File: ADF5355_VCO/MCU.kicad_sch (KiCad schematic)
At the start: 34 parts, among them SW2 SW_Push, SW3 SW_DPDT_x2, U2 STM32L433CCTx, Y1 8MHz, Y2 32kHz

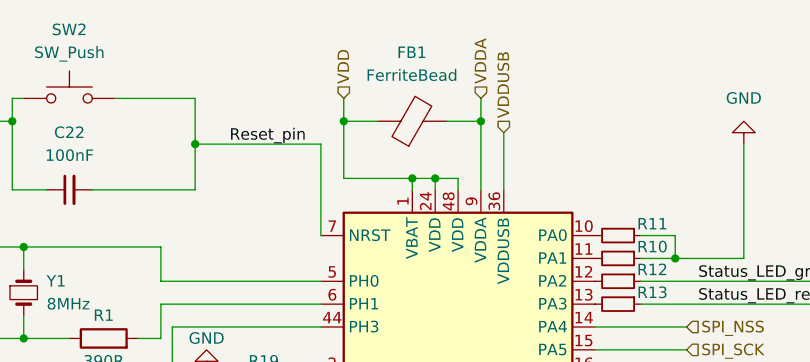
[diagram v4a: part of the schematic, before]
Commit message: Changed the power port
Changed all power ports to be global instead of them being hierarchical sheet pins
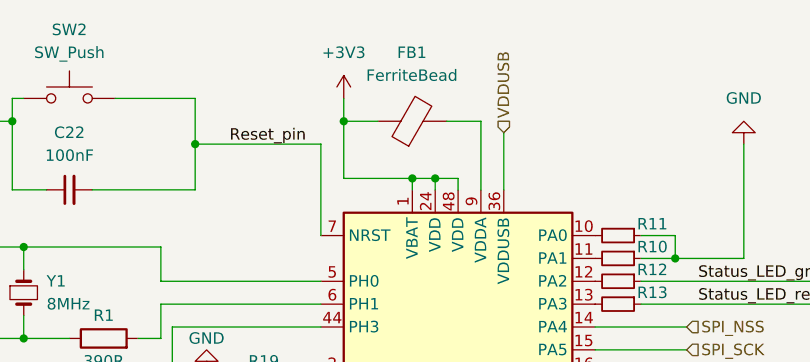
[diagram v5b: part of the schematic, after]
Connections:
- net VDD: no longer FB1.1, U2.1 (VBAT), U2.24 (VDD), U2.48 (VDD)
- net VDDA: no longer FB1.2, U2.9 (VDDA)
- new net: FB1.2, U2.9 (VDDA)
- new net +3V3: FB1.1, U2.1 (VBAT), U2.24 (VDD), U2.48 (VDD)
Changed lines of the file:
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@@
   (junction (at 30.48 165.1) (diameter 0) (color 0 0 0 0)
   )
-  (junction (at 121.92 50.8) (diameter 0) (color 0 0 0 0)
-  )
   (junction (at 40.64 172.72) (diameter 0) (color 0 0 0 0)
   )
@@
   )
   (wire (pts (xy 57.15 86.36) (xy 57.15 91.44))
-    (stroke (width 0) (type default))
-  )
-  (wire (pts (xy 121.92 48.26) (xy 121.92 50.8))
     (stroke (width 0) (type default))
   )
@@
     (effects (font (size 1.27 1.27)) (justify right))
   )
-  (hierarchical_label "VDDA" (shape input) (at 121.92 48.26 90) (fields_autoplaced)
-    (effects (font (size 1.27 1.27)) (justify left))
-  )
   (hierarchical_label "VDD" (shape input) (at 24.13 74.93 90) (fields_autoplaced)
     (effects (font (size 1.27 1.27)) (justify left))
   )
   (hierarchical_label "USB_DM" (shape input) (at 153.67 91.44 0) (fields_autoplaced)
-    (effects (font (size 1.27 1.27)) (justify left))
-  )
-  (hierarchical_label "VDD" (shape input) (at 106.68 48.26 90) (fields_autoplaced)
     (effects (font (size 1.27 1.27)) (justify left))
   )
@@
         )
       )
+    )
+  )
+  (symbol (lib_id "power:+3V3") (at 106.68 48.26 0) (unit 1)
+    (in_bom yes) (on_board yes) (dnp no) (fields_autoplaced)
+    (property "Reference" "#PWR041" (at 106.68 52.07 0)
+      (effects (font (size 1.27 1.27)) hide)
+    )
+    (property "Value" "+3V3" (at 106.68 43.18 0)
+      (effects (font (size 1.27 1.27)))
+    )
+    (property "Footprint" "" (at 106.68 48.26 0)
+      (effects (font (size 1.27 1.27)) hide)
+    )
+    (property "Datasheet" "" (at 106.68 48.26 0)
+      (effects (font (size 1.27 1.27)) hide)
+    )
+    (pin "1")
+    (instances
+      (project "ADF5355_VCO"
+        (path "/29349b68-071c-451b-9b1e-10b5ef7e12a6/8e6d62a1-615e-4e74-ad33-9284c4715f87"
+          (reference "#PWR041") (unit 1)
+        )
+      )

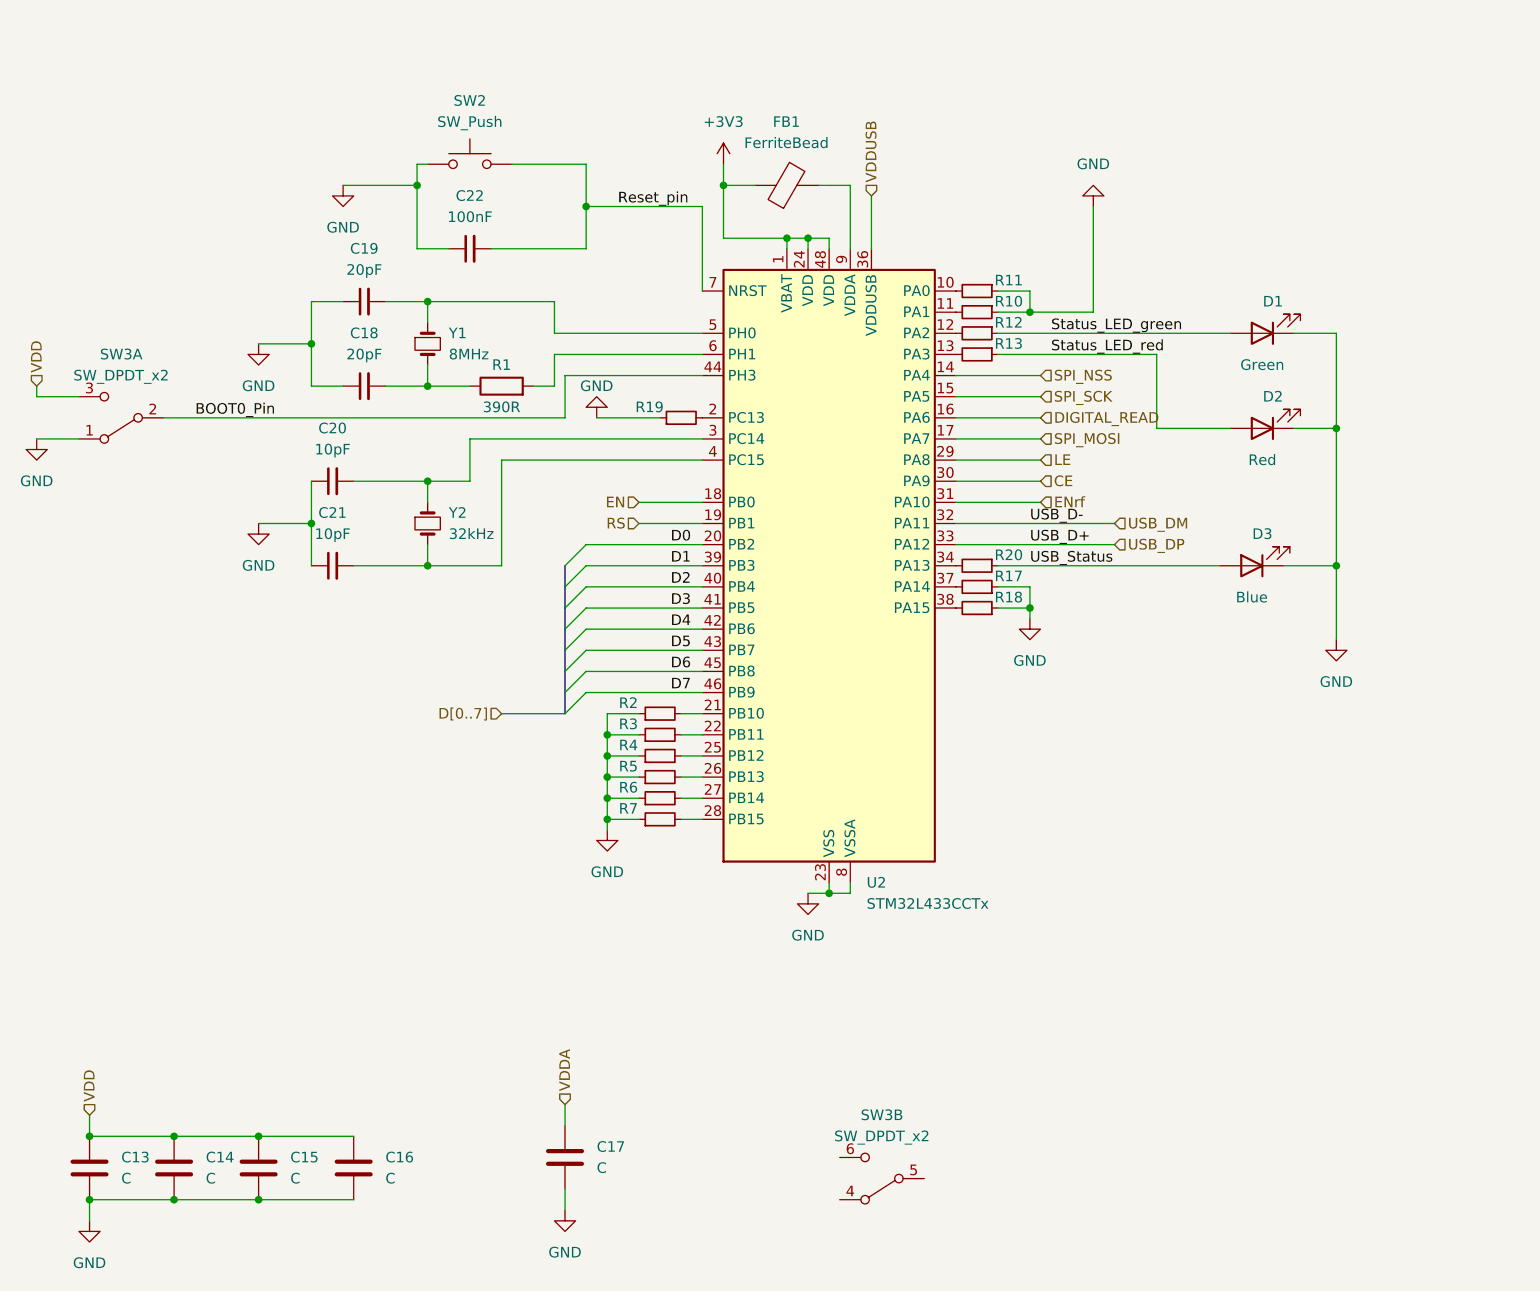
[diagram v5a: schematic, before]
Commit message: Added additional footprints and BOM
Added a bill of materials with most of the components.
Added footprints for more components
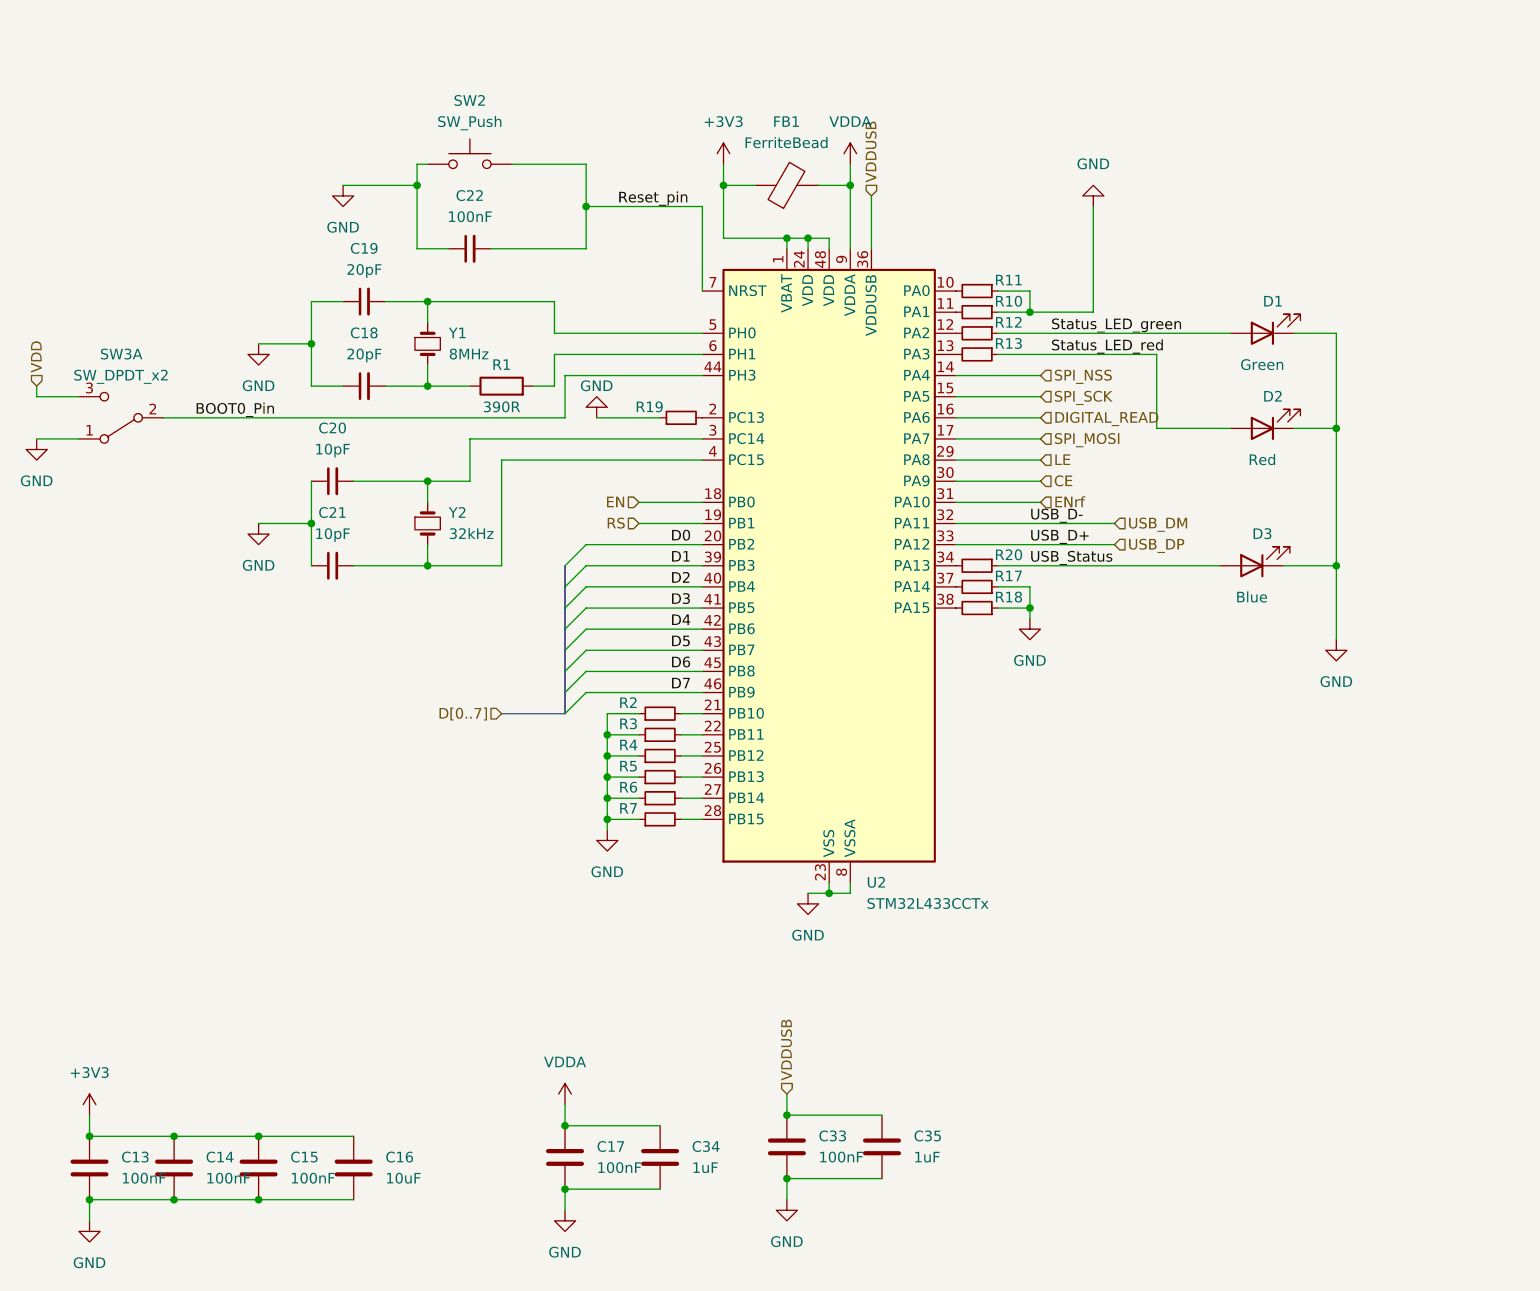
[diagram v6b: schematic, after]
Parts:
- removed unit 2 of SW3
- added C33: 100nF, Capacitor_SMD:C_0603_1608Metric_Pad1.08x0.95mm_HandSolder, symbol Device:C
- added C34, C35: 1uF, Capacitor_SMD:C_0603_1608Metric_Pad1.08x0.95mm_HandSolder, symbol Device:C
- C13, C14, C15, C17: value C -> 100nF; footprint (none) -> Capacitor_SMD:C_0603_1608Metric_Pad1.08x0.95mm_HandSolder
- C16: value C -> 10uF; footprint (none) -> Capacitor_SMD:C_0603_1608Metric_Pad1.08x0.95mm_HandSolder
- C22: footprint (none) -> Capacitor_SMD:C_0603_1608Metric_Pad1.08x0.95mm_HandSolder
- R10, R11, R12, R13, R17, R18, R19, R2, R20, R3, R4, R5, R6, R7: footprint (none) -> Resistor_SMD:R_0603_1608Metric_Pad0.98x0.95mm_HandSolder
- Y2: footprint (none) -> Crystal:Crystal_Round_D3.0mm_Vertical
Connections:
- net +3V3: now also C13.1, C14.1, C15.1, C16.1
- net GND: now also C33.2, C34.2, C35.2
- net VDD: no longer C13.1, C14.1, C15.1, C16.1
- net VDDA: now also FB1.2, U2.9 (VDDA), C34.1
- net VDDUSB: now also C33.1, C35.1
